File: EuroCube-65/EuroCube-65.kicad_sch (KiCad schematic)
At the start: 103 parts, among them CON1 SERIAL PORT, CON2 PARALLEL PORT, CON3 EXPANSION BUS, IC1 6551A, IC10 GAL16V8, IC11 6522, IC12 6502, IC13 7660, IC2 26LS30, IC3 M3000 CLOCK, IC4 26LS32, IC5 74LS04, IC7 74LS00, IC8 74HCT132, IC9 GAL16V8, T1 BC547, T2 2N7000, T3 2N3906, X1 1.843MHz, X2 32.768kHz, X3 1MHz

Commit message: Update sch
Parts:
- TP1: value ~ -> RXC
- TP3: value ~ -> ~{DTR}
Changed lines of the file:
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@@
 			)
 		)
-		(property "Value" "~"
+		(property "Value" "RXC"
 			(at 128.778 185.6048 90)
 			(effects
@@
 					(size 1.27 1.27)
 				)
+				(hide yes)
 			)
 		)
@@
 			)
 		)
-		(property "Value" "~"
+		(property "Value" "~{DTR}"
 			(at 128.778 188.1448 90)
 			(effects
@@
 					(size 1.27 1.27)
 				)
+				(hide yes)
 			)
 		)

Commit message: Minor updates to schematic/BOM
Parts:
- removed L4: ~, symbol Jumper:Jumper_2_Small_Open
- added L4: ~, symbol Jumper:Jumper_2_Small_Bridged
- added TP5: VCB, symbol Connector:TestPoint
- C10, C11, C12, C13: value ~ -> 47p
- IC3: value M3000 CLOCK -> M3002
- R14, R9: value ~ -> 240
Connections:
- net VCB: now also TP5.1
- net at CON2.23 (Pin_23), D1.2 (A), L10.2 (B)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: now also L4.2 (B)
- net at IC1.12 (RXD), IC4.5: now also L4.1 (A)
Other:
- note added: "Errors on original schematics: 1. IC1 pin 28 R/~{W} connected to IRQ instead of B R/~{W} 2. C8,10, 13, 16 not fitted according to schematic note, but C8 trimmer is 3. C10, 11, 12, 13 vaues missing from BOM (47p)"
- note removed: "Errors on original schematic: 1. IC1 pin 28 R/~{W} connected to IRQ instead of B R/~{W} 2. C8,10, 13, 16 not fitted according to schematic note, but C8 trimmer is 3. C10, 11, 12, 13 vaues missing from BOM"
- company: (none) -> steve@croz.co.uk
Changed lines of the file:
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@@
 		(date "2024-11-16")
 		(rev "ISSUE 8")
+		(company "steve@croz.co.uk")
+		(comment 1 "Based on issue 7 with addition of R31 pullup")
 	)
 	(junction
@@
 	)
 	(junction
+		(at 190.5 203.2)
+		(diameter 0)
+		(color 0 0 0 0)
+	)
+	(junction
 		(at 312.42 135.89)
 		(diameter 0)
@@
 		)
 	)
+	(wire
+		(pts
+			(xy 190.5 203.2) (xy 194.31 203.2)
+		)
+		(stroke
+			(width 0)
+			(type default)
+		)
+	)
 	(bus
 		(pts
@@
 	(wire
 		(pts
-			(xy 179.07 203.2) (xy 194.31 203.2)
+			(xy 179.07 203.2) (xy 190.5 203.2)
 		)
 		(stroke
@@
 	(wire
 		(pts
+			(xy 190.5 200.66) (xy 190.5 203.2)
+		)
+		(stroke
+			(width 0)
+			(type default)
+		)
+	)
+	(wire
+		(pts
 			(xy 137.16 238.76) (xy 137.16 232.41)
 		)
@@
 		)
 	)
-	(text "Errors on original schematic:\n\n1. IC1 pin 28 R/~{W} connected to IRQ instead of B R/~{W}\n2. C8,10, 13, 16 not fitted according to schematic note, but C8 trimmer is\n3. C10, 11, 12, 13 vaues missing from BOM"
+	(text "Errors on original schematics:\n\n1. IC1 pin 28 R/~{W} connected to IRQ instead of B R/~{W}\n2. C8,10, 13, 16 not fitted according to schematic note, but C8 trimmer is\n3. C10, 11, 12, 13 vaues missing from BOM (47p)"
 		(exclude_from_sim no)
 		(at 253.746 204.724 0)
@@
 		)
 	)
-	(label "VCB"
-		(at 186.69 203.2 0)
-		(fields_autoplaced yes)
-		(effects
-			(font
-				(size 1.27 1.27)
-			)
-			(justify left bottom)
-		)
-	)
 	(label "~{WDS}"
 		(at 231.14 49.53 0)
@@
 			)
 		)
-		(property "Value" "~"
+		(property "Value" "47p"
 			(at 107.9563 180.8677 90)
 			(effects
@@
 					(size 1.27 1.27)
 				)
+				(hide yes)
 			)
 		)
@@
 		(dnp no)
 		(property "Reference" "C16"
-			(at 188.214 204.47 0)
+			(at 188.468 205.232 0)
 			(effects
 				(font
@@
 		)
 		(property "Value" "2.2u"
-			(at 188.468 206.502 0)
+			(at 188.468 207.01 0)
 			(effects
 				(font
@@
 		(dnp no)
 		(property "Reference" "L10"
-			(at 120.65 229.87 0)
+			(at 120.65 233.934 0)
 			(effects
 				(font
@@
 		)
 		(property "Value" "~{RESET}"
-			(at 113.03 232.41 0)
+			(at 120.904 229.87 0)
 			(effects
 				(font
@@
 			)
 		)
-		(property "Value" "~"
+		(property "Value" "47p"
 			(at 107.9563 168.9108 90)
 			(effects
@@
 					(size 1.27 1.27)
 				)
+				(hide yes)
 			)
 		)
@@
 	)
 	(symbol
+		(lib_id "Jumper:Jumper_2_Small_Bridged")
+		(at 125.73 207.01 270)
+		(unit 1)
+		(exclude_from_sim yes)
+		(in_bom yes)
+		(on_board yes)
+		(dnp no)
+		(property "Reference" "L4"
+			(at 124.206 207.01 90)
+			(effects
+				(font
+					(size 1.27 1.27)
+				)
+			)
+		)
+		(property "Value" "~"
+			(at 127.8928 207.01 0)
+			(effects
+				(font
+					(size 1.27 1.27)
+				)
+			)
+		)
+		(property "Footprint" ""
+			(at 125.73 207.01 0)
+			(effects
+				(font
+					(size 1.27 1.27)
+				)
+				(hide yes)
+			)
+		)
+		(property "Datasheet" "~"
+			(at 125.73 207.01 0)
+			(effects
+				(font
+					(size 1.27 1.27)
+				)
+				(hide yes)
+			)
+		)
+		(property "Description" "Jumper, 2-pole, small symbol, bridged"
+			(at 125.73 207.01 0)
+			(effects
+				(font
+					(size 1.27 1.27)
+				)
+				(hide yes)
+			)
+		)
+		(pin "1"
+		)
+		(pin "2"
+		)
+		(instances
+			(project "EuroCube-65"
+				(path "/2a966873-1bce-441e-b1e5-16428638ef47"
+					(reference "L4")
+					(unit 1)
+				)
+			)
+		)
+	)
+	(symbol
 		(lib_id "Transistor_BJT:BC547")
 		(at 215.9 233.68 0)
@@
 			)
 		)
-		(property "Value" "~"
+		(property "Value" "240"
 			(at 80.518 207.264 90)
 			(effects
@@
 	)
 	(symbol
-		(lib_id "Jumper:Jumper_2_Small_Open")
-		(at 125.73 207.01 270)
-		(unit 1)
-		(exclude_from_sim yes)
-		(in_bom yes)
-		(on_board yes)
-		(dnp no)
-		(property "Reference" "L4"
-			(at 124.46 207.01 90)
-			(effects
-				(font
-					(size 1.27 1.27)
-				)
-			)
-		)
-		(property "Value" "~"
-			(at 128.5961 207.01 0)
-			(effects
-				(font
-					(size 1.27 1.27)
-				)
-			)
-		)
-		(property "Footprint" ""
-			(at 125.73 207.01 0)
-			(effects
-				(font
-					(size 1.27 1.27)
-				)
-				(hide yes)
-			)
-		)
-		(property "Datasheet" "~"
-			(at 125.73 207.01 0)
-			(effects
-				(font
-					(size 1.27 1.27)
-				)
-				(hide yes)
-			)
-		)
-		(property "Description" "Jumper, 2-pole, small symbol, open"
-			(at 125.73 207.01 0)
-			(effects
-				(font
-					(size 1.27 1.27)
-				)
-				(hide yes)
-			)
-		)
-		(pin "1"
-		)
-		(pin "2"
-		)
-		(instances
-			(project "EuroCube-65"
-				(path "/2a966873-1bce-441e-b1e5-16428638ef47"
-					(reference "L4")
-					(unit 1)
-				)
-			)
-		)
-	)
-	(symbol
 		(lib_id "power:GND")
 		(at 265.43 120.65 0)
@@
 			)
 		)
-		(property "Value" "~"
+		(property "Value" "47p"
 			(at 107.9563 163.0877 90)
 			(effects
@@
 					(size 1.27 1.27)
 				)
+				(hide yes)
 			)
 		)
@@
 	)
 	(symbol
+		(lib_id "Connector:TestPoint")
+		(at 190.5 200.66 90)
+		(unit 1)
+		(exclude_from_sim no)
+		(in_bom no)
+		(on_board yes)
+		(dnp no)
+		(property "Reference" "TP5"
+			(at 184.404 199.644 90)
+			(effects
+				(font
+					(size 1.27 1.27)
+				)
+			)
+		)
+		(property "Value" "VCB"
+			(at 184.404 201.676 90)
+			(effects
+				(font
+					(size 1.27 1.27)
+				)
+			)
+		)
+		(property "Footprint" ""
+			(at 190.5 195.58 0)
+			(effects
+				(font
+					(size 1.27 1.27)
+				)
+				(hide yes)
+			)
+		)
+		(property "Datasheet" "~"
+			(at 190.5 195.58 0)
+			(effects
+				(font
+					(size 1.27 1.27)
+				)
+				(hide yes)
+			)
+		)
+		(property "Description" "test point"
+			(at 190.5 200.66 0)
+			(effects
+				(font
+					(size 1.27 1.27)
+				)
+				(hide yes)
+			)
+		)
+		(pin "1"
+		)
+		(instances
+			(project "EuroCube-65"
+				(path "/2a966873-1bce-441e-b1e5-16428638ef47"
+					(reference "TP5")
+					(unit 1)
+				)
+			)
+		)
+	)
+	(symbol
 		(lib_id "Device:D_Small")
 		(at 200.66 231.14 270)
@@
 			)
 		)
-		(property "Value" "~"
+		(property "Value" "47p"
 			(at 107.9563 150.3877 90)
 			(effects
@@
 					(size 1.27 1.27)
 				)
+				(hide yes)
 			)
 		)
@@
 			)
 		)
-		(property "Value" "M3000 CLOCK"
-			(at 253.492 157.48 0)
+		(property "Value" "M3002"
+			(at 257.048 157.48 0)
 			(effects
 				(font
@@
 			)
 		)
-		(property "Value" "~"
+		(property "Value" "240"
 			(at 80.518 195.834 90)
 			(effects
@@
 					(size 1.27 1.27)
 				)
+				(hide yes)
 			)
 		)

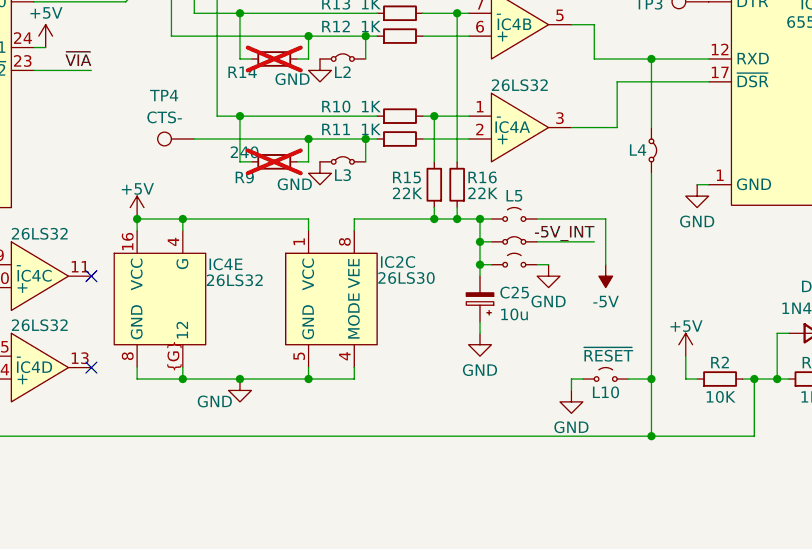
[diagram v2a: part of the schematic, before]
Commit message: Added footprints, started laying out
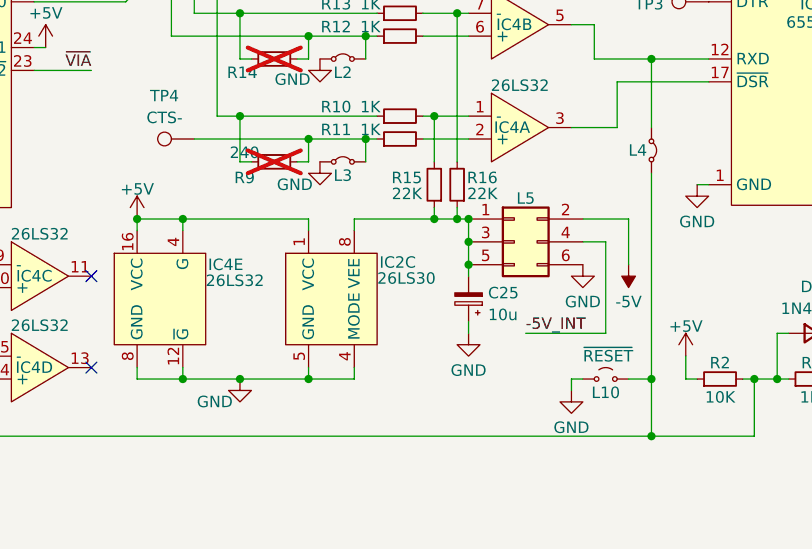
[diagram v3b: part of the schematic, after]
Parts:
- removed L5, L52: ~, symbol Jumper:Jumper_2_Small_Open
- removed L51: SERIAL CONFIG, symbol Jumper:Jumper_2_Small_Bridged
- added L5: ~, Connector_PinHeader_2.54mm:PinHeader_2x03_P2.54mm_Vertical, symbol Connector_Generic:Conn_02x03_Odd_Even
- B1: footprint (none) -> EuroCube-65:Battery
- C1, C10, C11, C12, C13, C15, C17, C18, C19, C20, C21, C22, C26, C27, C28, C29, C30, C4, C6, C7, C9: footprint (none) -> Capacitor_THT:C_Disc_D3.4mm_W2.1mm_P2.50mm
- C16, C23, C24, C25: footprint (none) -> Capacitor_THT:CP_Radial_D5.0mm_P2.00mm
- C8: footprint (none) -> EuroCube-65:Trimmer_small
- CON1: footprint (none) -> EuroCube-65:DIN-7
- CON2: footprint (none) -> Connector_IDC:IDC-Header_2x13-1MP_P2.54mm_Latch_Horizontal
- CON3: footprint (none) -> Connector_DIN:DIN41612_B_2x32_Male_Horizontal_THT
- D1, D2, D3, D4: footprint (none) -> Diode_THT:D_DO-35_SOD27_P7.62mm_Horizontal
- IC1, M0, M1, M2, M3: footprint (none) -> Package_DIP:DIP-28_W15.24mm_Socket
- IC10, IC9: footprint (none) -> Package_DIP:DIP-20_W7.62mm_Socket
- IC11, IC12: footprint (none) -> Package_DIP:DIP-40_W15.24mm_Socket
- IC13: footprint (none) -> Package_DIP:DIP-8_W7.62mm_Socket
- IC2, IC3, IC4: footprint (none) -> Package_DIP:DIP-16_W7.62mm_Socket
- IC5, IC7, IC8: footprint (none) -> Package_DIP:DIP-14_W7.62mm_Socket
- L10: footprint (none) -> Connector_PinHeader_2.54mm:PinHeader_1x02_P2.54mm_Vertical
- L2, L3, L4, L6, L7, L8, L9: footprint (none) -> EuroCube-65:PinHeader_1x02_P2.54mm_V_Tight
- R10, R11, R12, R13, R14, R15, R16, R17, R18, R19, R23, R28, R29, R30, R31, R9: footprint (none) -> Resistor_THT:R_Axial_DIN0207_L6.3mm_D2.5mm_P2.54mm_Vertical
- R2, R24, R25, R26, R27, R3, R4, R5, R6, R7, R8: footprint (none) -> Resistor_THT:R_Axial_DIN0207_L6.3mm_D2.5mm_P7.62mm_Horizontal
- S1, S3, S4: footprint (none) -> EuroCube-65:ConfigBlock_2x09_P2.54mm_Vertical
- S2: footprint (none) -> Package_DIP:CERDIP-18_W7.62mm_SideBrazed_Socket
- TP1, TP2, TP3, TP4, TP5: footprint (none) -> TestPoint:TestPoint_THTPad_D1.5mm_Drill0.7mm
- X1, X3: footprint (none) -> Crystal:Crystal_HC49-U_Vertical
- X2: footprint (none) -> Crystal:Crystal_C38-LF_D3.0mm_L8.0mm_Horizontal
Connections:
- net -5V: now also L5.2 (Pin_2)
- net -5V_INT: now also L5.4 (Pin_4)
- net GND: now also IC4.12 (~{G}), L5.6 (Pin_6); no longer IC4.~{G} (12)
- net at C25.2, IC2.8 (VEE), R15.1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: now also L5.1 (Pin_1), L5.3 (Pin_3), L5.5 (Pin_5)
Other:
- moved on the sheet: C25

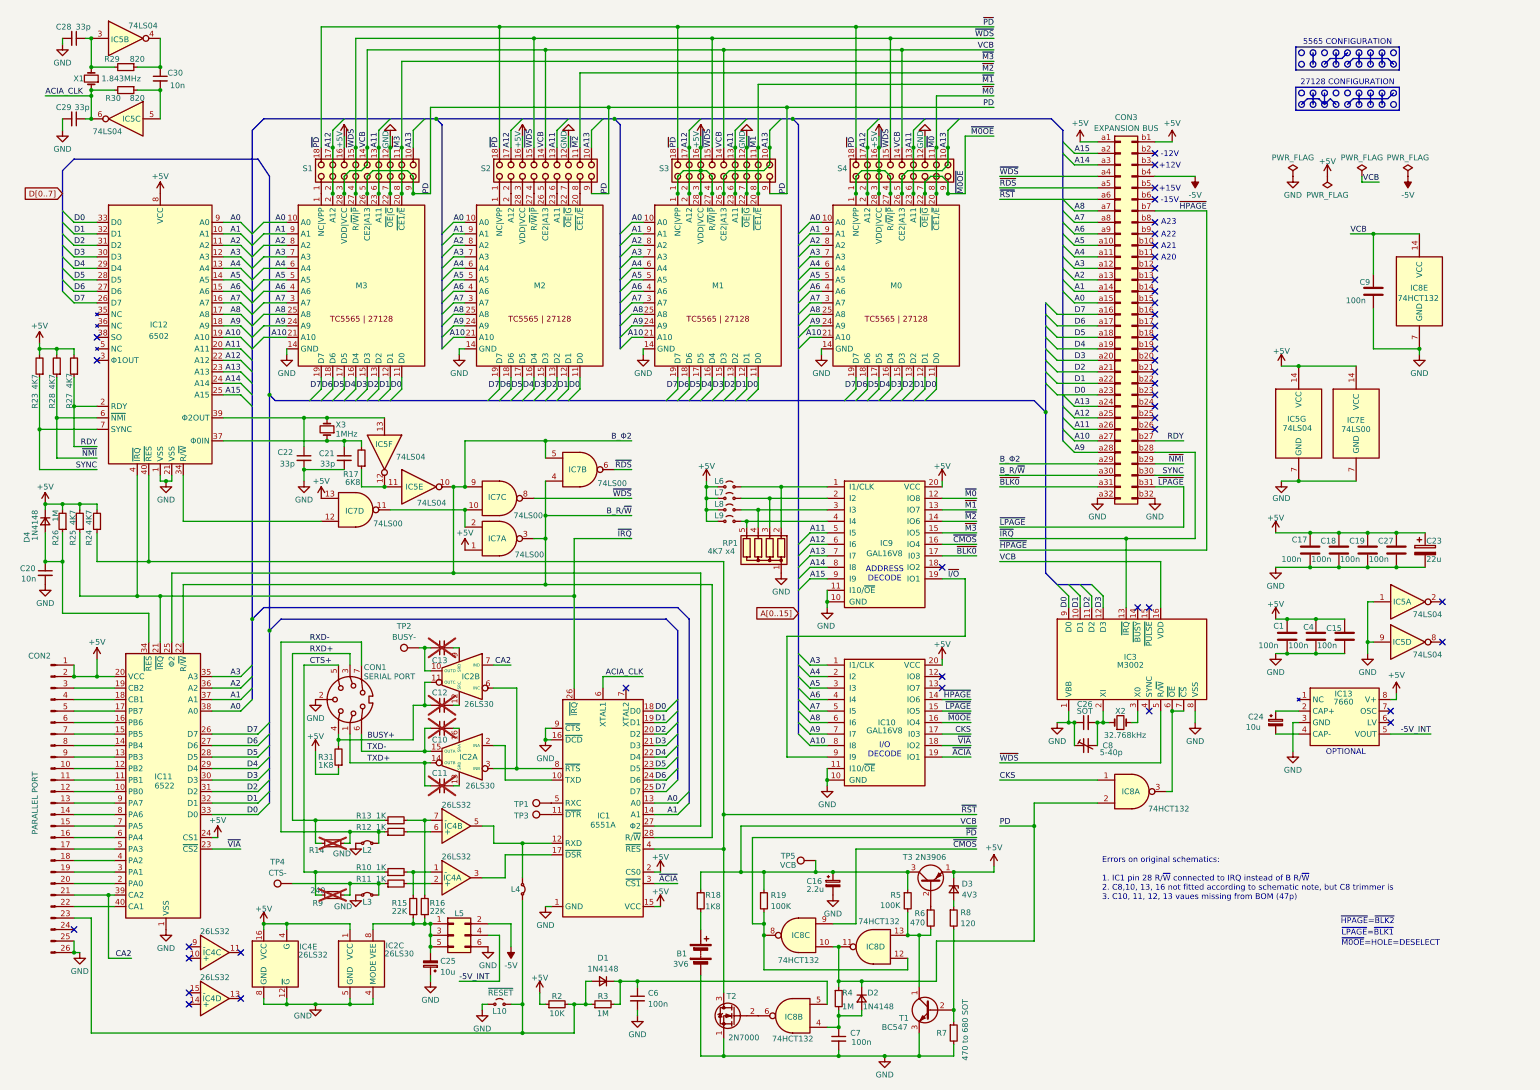
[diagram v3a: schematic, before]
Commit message: Minor footprint tweaks
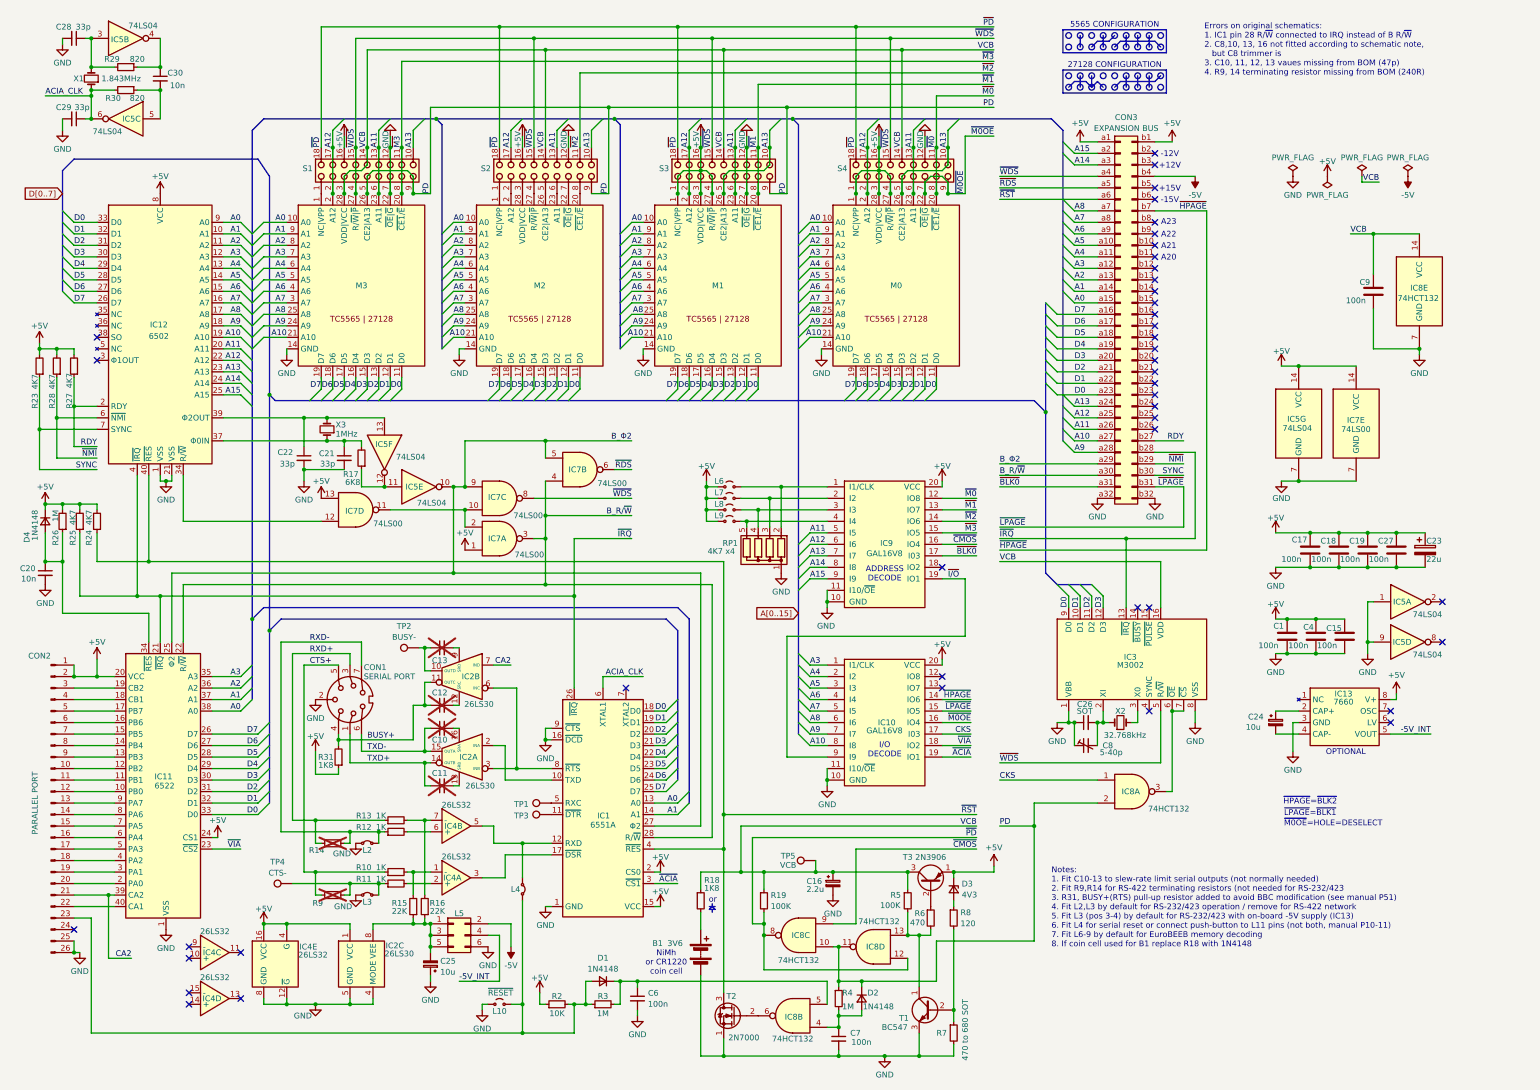
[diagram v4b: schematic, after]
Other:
- note added: "Errors on original schematics: 1. IC1 pin 28 R/~{W} connected to IRQ instead of B R/~{W} 2. C8,10, 13, 16 not fitted according to schematic note, but C8 trimmer is 3. C10, 11, 12, 13 vaues missing from BOM (47p) 4. R9, 14 terminating resistor missing from BOM (240R)"
- note added: "NiMh or CR1220 coin cell"
- note added: "Notes: 1. Fit C10-13 to slew-rate limit serial outputs (not normally needed) 2. Fit R9,R14 for RS-422 terminating resistors (not needed for RS-232/423 3. R31, BUSY+(RTS) pull-up resistor added to avoid BBC modification (see manual P51) 4. Fit L2,L3 by default for RS-232/423 operation / remove for RS-422 network 5. Fit L3 (pos 3-4) by default for RS-232/423 with on-board -5V supply (IC13) 6. Fit L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"
- note added: "or"
- note removed: "Errors on original schematics: 1. IC1 pin 28 R/~{W} connected to IRQ instead of B R/~{W} 2. C8,10, 13, 16 not fitted according to schematic note, but C8 trimmer is 3. C10, 11, 12, 13 vaues missing from BOM (47p)"
